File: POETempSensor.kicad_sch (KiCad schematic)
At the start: 0 parts

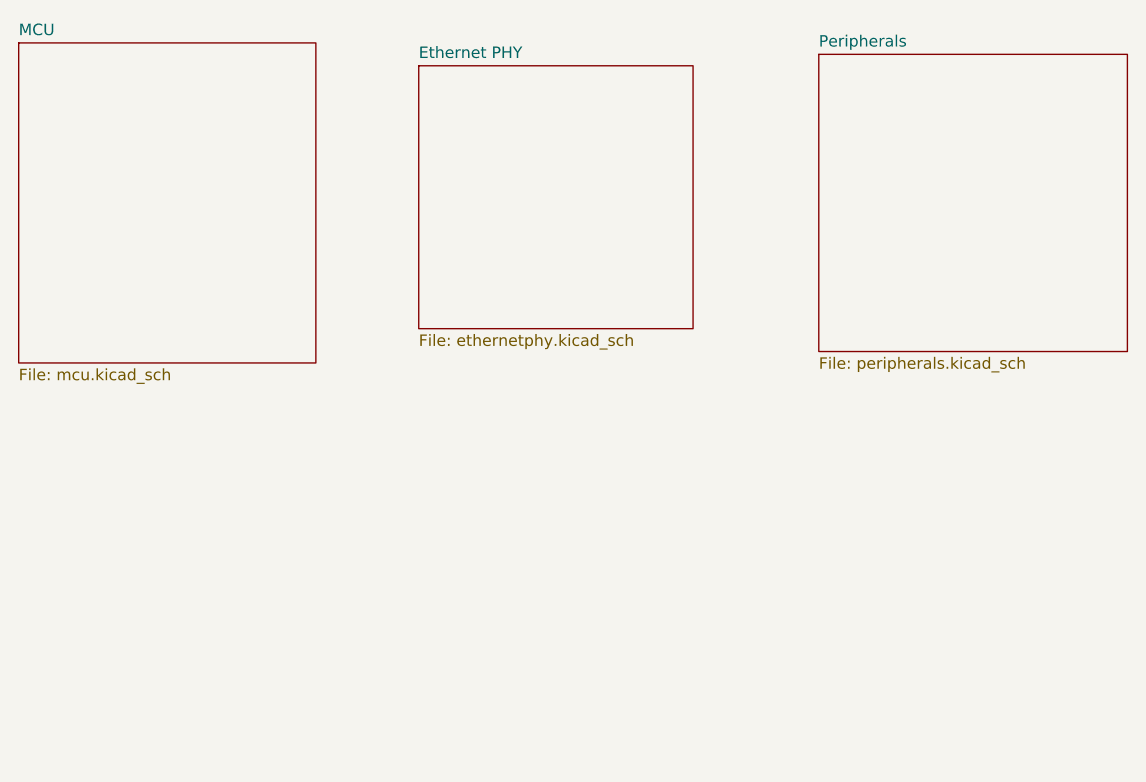
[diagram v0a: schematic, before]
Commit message: Add power sheet and update schematic connections
Added a new power sheet to the project and updated the main schematic to include connections for power, MCU, peripherals, and Ethernet PHY. Also added backup files and updated the Ethernet PHY schematic with symbol definitions and pin mappings.
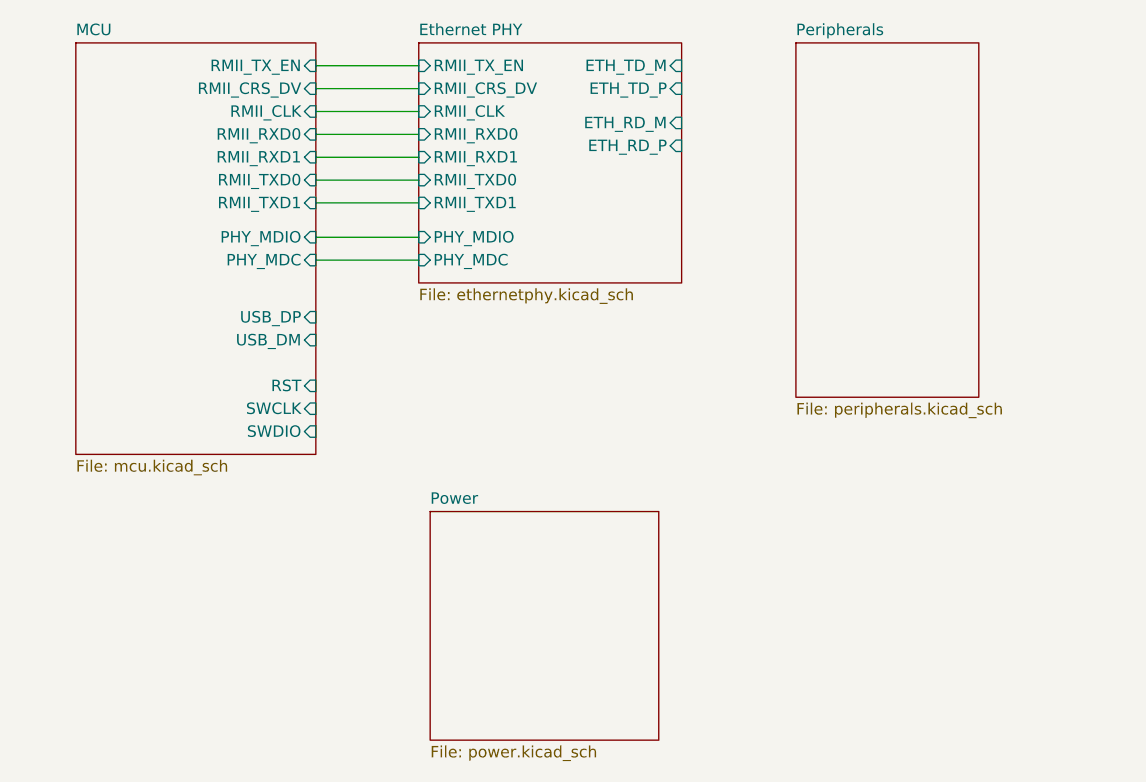
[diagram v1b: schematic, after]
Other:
- added sheet Power (power.kicad_sch)
- sheet Ethernet PHY ports: added ETH_RD_M, ETH_RD_P, ETH_TD_M, ETH_TD_P, PHY_MDC, PHY_MDIO, RMII_CLK, RMII_CRS_DV, RMII_RXD0, RMII_RXD1, RMII_TXD0, RMII_TXD1, RMII_TX_EN; removed none
- sheet MCU ports: added PHY_MDC, PHY_MDIO, RMII_CLK, RMII_CRS_DV, RMII_RXD0, RMII_RXD1, RMII_TXD0, RMII_TXD1, RMII_TX_EN, RST, SWCLK, SWDIO, USB_DM, USB_DP; removed none
